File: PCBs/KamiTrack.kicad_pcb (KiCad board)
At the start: 2 copper layers, 78.5 x 20.6 mm, 65 parts, among them J1 Conn_01x02_Female, J2 Conn_01x04_Female, J3 Conn_01x02_Female, J4 Conn_01x08_Female, J5 Conn_01x02_Female, P1 USB_C_Plug_USB2.0, SW1 Option/FLASH Switch, SW2 Cali Switch, SW3 SW_SPDT MAIN POWER, U1 ME6211C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

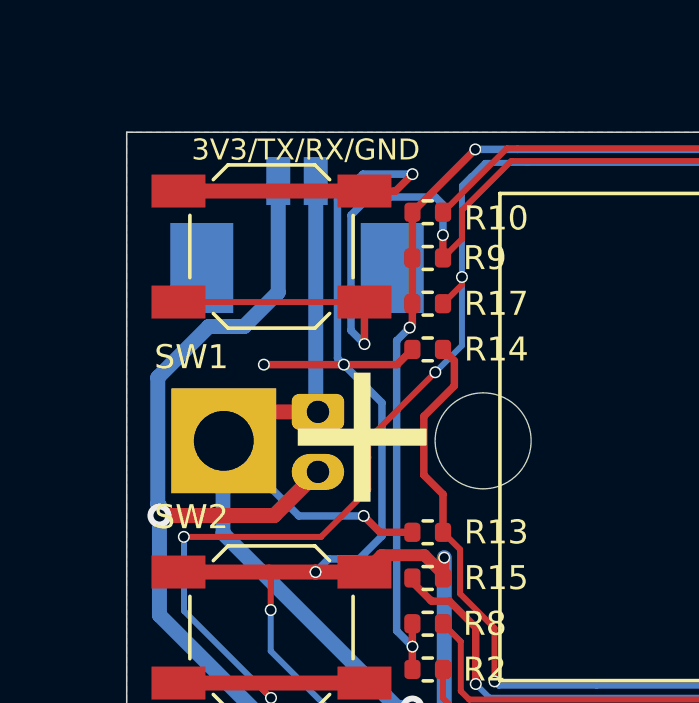
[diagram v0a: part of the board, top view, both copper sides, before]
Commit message: Rename to kamitrack
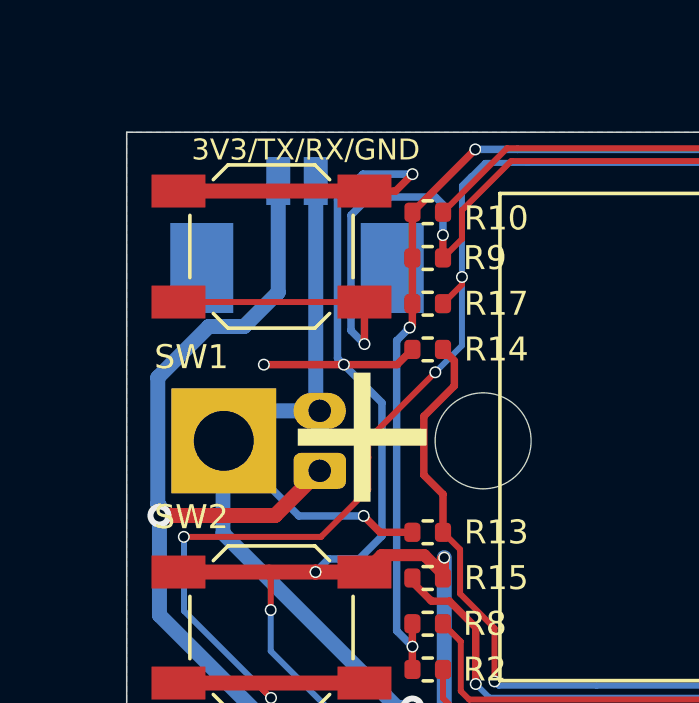
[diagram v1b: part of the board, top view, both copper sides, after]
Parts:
- J1: footprint Connector_JST:JST_PH_S2B-PH-K_1x02_P2.00mm_Horizontal -> Connector_JST:JST_PH_B2B-PH-K_1x02_P2.00mm_Vertical
- moved J1 1.97 mm to (96.2, 66.5), turned to 90 degrees
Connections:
- J1 pad 1: BATT+ -> BATT-
- J1 pad 2: BATT- -> BATT+
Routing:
- net BATT+: track 183.8 -> 185.2 mm
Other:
- board text added: "+ -"

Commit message: add JLCPCB_CORRECTION
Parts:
- J1: footprint Connector_JST:JST_PH_B2B-PH-K_1x02_P2.00mm_Vertical -> Connector_JST:JST_PH_S2B-PH-K_1x02_P2.00mm_Horizontal; moved to F.Cu
- moved J1 1.97 mm to (96.8, 64.6), turned to -90 degrees
- moved C14 0.69 mm to (145.2, 68.7)
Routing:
- net GND: track 446.8 -> 439.6 mm
- net BATT+: track 185.2 -> 190.6 mm, vias 11 -> 12
- net Net-(C14-Pad1): track 3.26 -> 4.84 mm
